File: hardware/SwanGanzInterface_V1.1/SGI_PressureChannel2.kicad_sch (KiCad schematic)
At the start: 18 parts, among them J6 Conn_01x04_Pin, U12 INA122D, U13 OPA2350

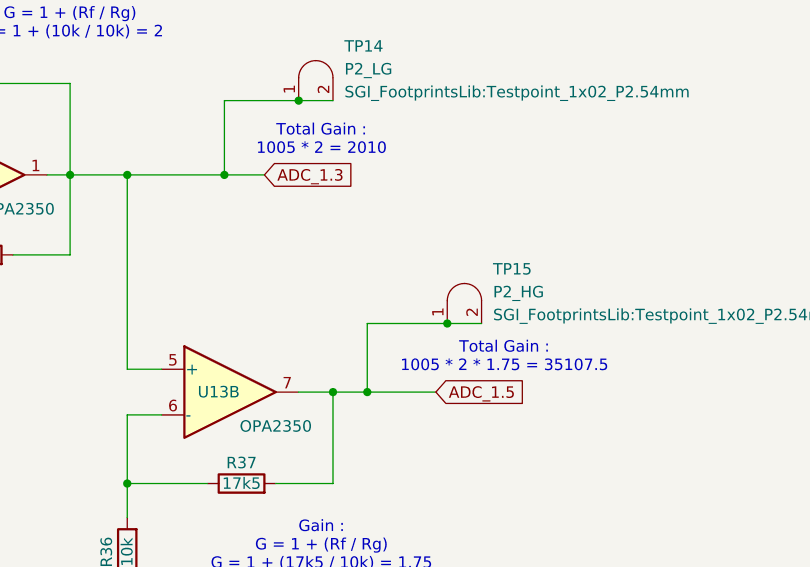
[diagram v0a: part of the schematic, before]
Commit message: Pin Allocation, updated schematic with new pins, reassigned
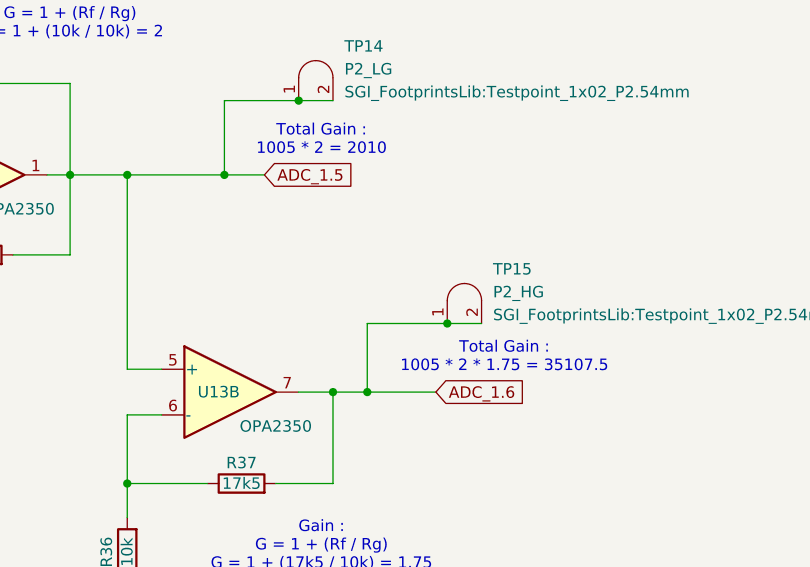
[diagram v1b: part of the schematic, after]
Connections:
- net ADC_1.3 is gone; now on net ADC_1.5: C20.2, R35.2, TP14.1 (A), TP14.2 (B), U13.1, U13.5 (+)
- net ADC_1.5: no longer R37.2, TP15.1 (A), TP15.2 (B), U13.7
- new net ADC_1.6: R37.2, TP15.1 (A), TP15.2 (B), U13.7
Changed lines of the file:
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@@
 		)
 	)
-	(global_label "ADC_1.5"
+	(global_label "ADC_1.6"
 		(shape input)
 		(at 201.93 88.9 0)
@@
 		)
 	)
-	(global_label "ADC_1.3"
+	(global_label "ADC_1.5"
 		(shape input)
 		(at 182.88 64.77 0)

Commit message: Hooked up MSP
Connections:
- net ADC_1.5 renamed P2_LG_ADC_1.5
- net ADC_1.6 renamed P2_HG_ADC_1.6
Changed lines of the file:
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@@
 		)
 	)
-	(global_label "ADC_1.6"
+	(global_label "P2_HG_ADC_1.6"
 		(shape input)
 		(at 201.93 88.9 0)
@@
 		)
 		(property "Intersheetrefs" "${INTERSHEET_REFS}"
-			(at 212.5352 88.9 0)
+			(at 219.5504 88.9 0)
 			(effects
 				(font
@@
 		)
 	)
-	(global_label "ADC_1.5"
+	(global_label "P2_LG_ADC_1.5"
 		(shape input)
 		(at 182.88 64.77 0)
@@
 		)
 		(property "Intersheetrefs" "${INTERSHEET_REFS}"
-			(at 193.4852 64.77 0)
+			(at 200.198 64.77 0)
 			(effects
 				(font

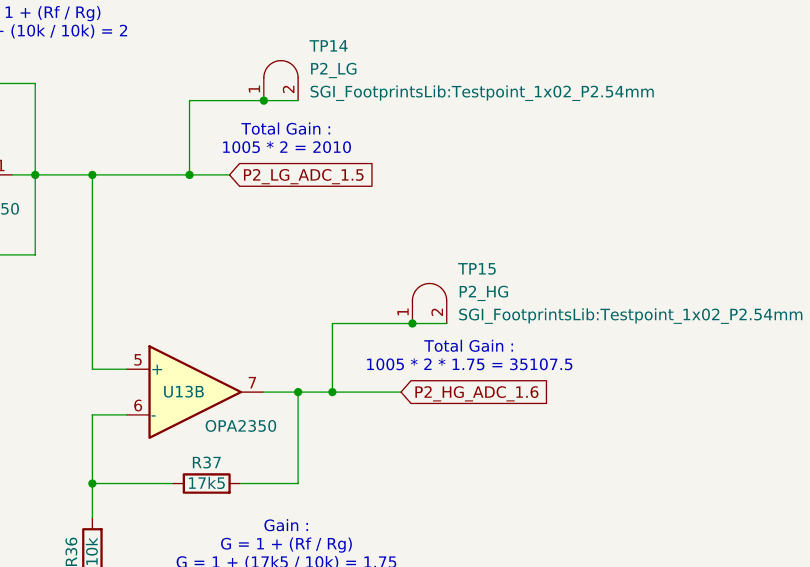
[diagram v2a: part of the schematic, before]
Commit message: Started converting things to use touch screen chip
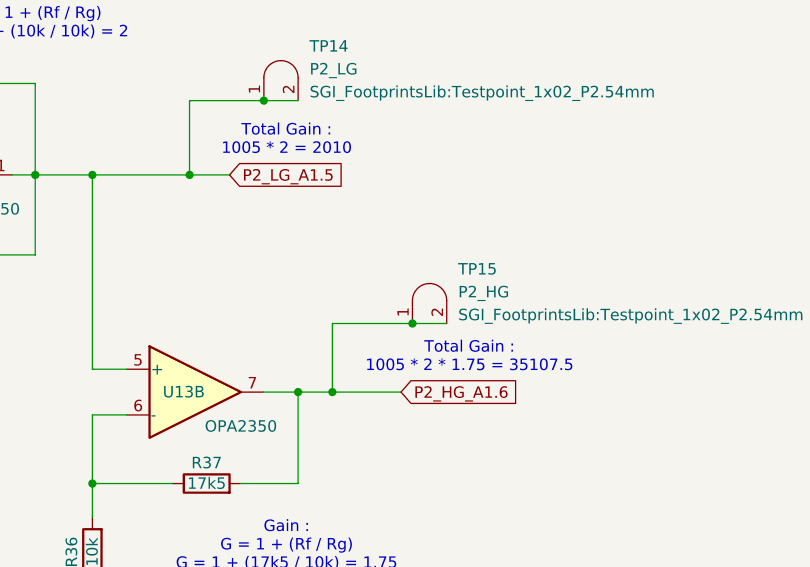
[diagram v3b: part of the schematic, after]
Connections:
- net P2_HG_ADC_1.6 renamed P2_HG_A1.6
- net P2_LG_ADC_1.5 renamed P2_LG_A1.5
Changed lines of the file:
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@@
 		)
 	)
-	(global_label "P2_HG_ADC_1.6"
+	(global_label "P2_HG_A1.6"
 		(shape input)
 		(at 201.93 88.9 0)
@@
 		)
 		(property "Intersheetrefs" "${INTERSHEET_REFS}"
-			(at 219.5504 88.9 0)
+			(at 216.0428 88.9 0)
 			(effects
 				(font
@@
 		)
 	)
-	(global_label "P2_LG_ADC_1.5"
+	(global_label "P2_LG_A1.5"
 		(shape input)
 		(at 182.88 64.77 0)
@@
 		)
 		(property "Intersheetrefs" "${INTERSHEET_REFS}"
-			(at 200.198 64.77 0)
+			(at 196.6904 64.77 0)
 			(effects
 				(font

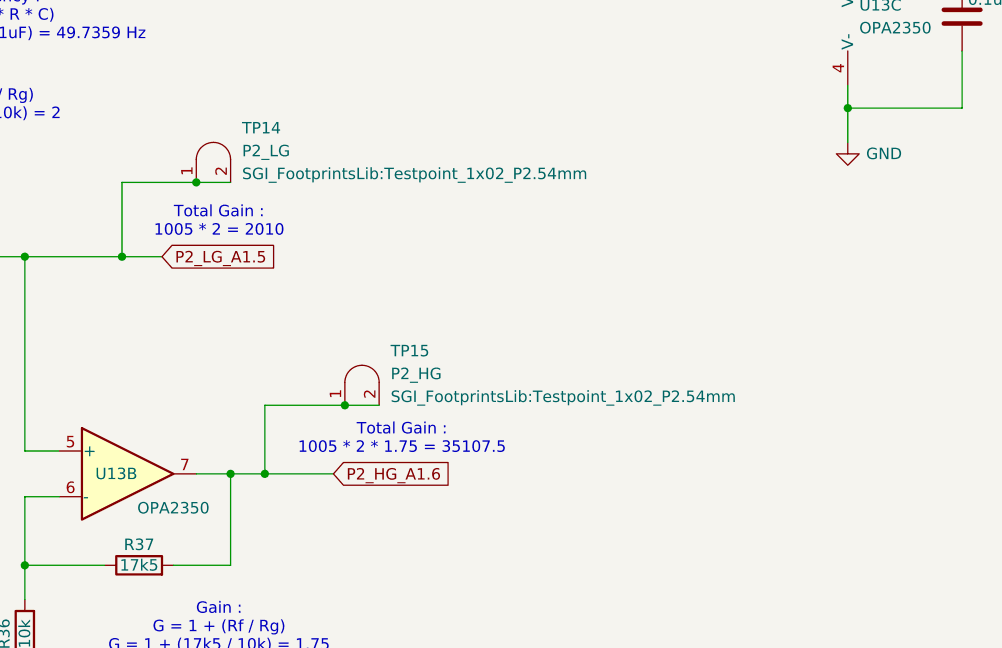
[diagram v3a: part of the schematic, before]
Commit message: Got 64 pin MSP symbol and footprint and started implementation
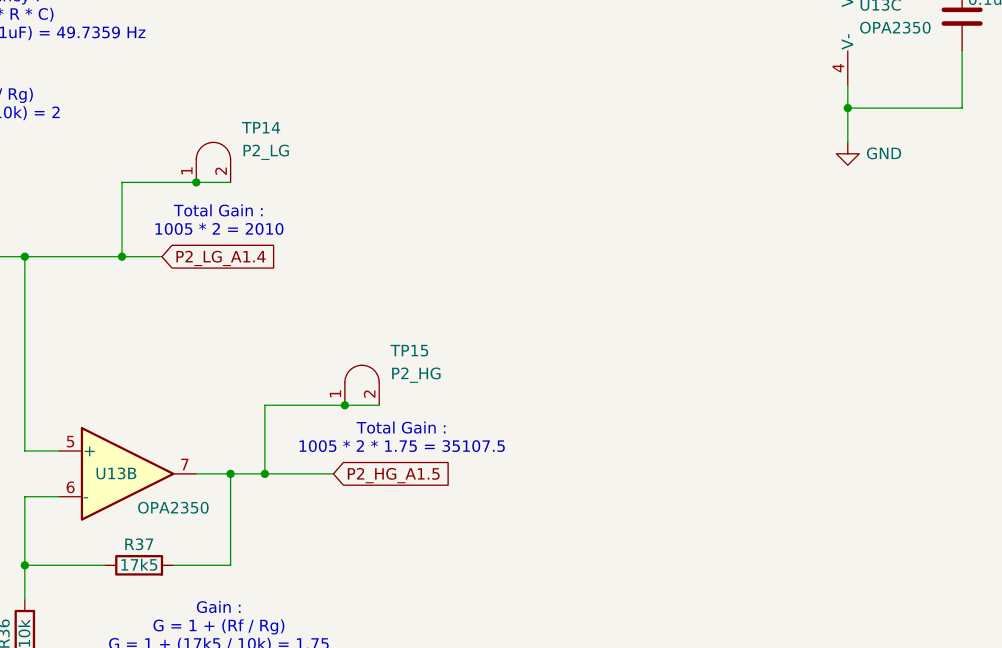
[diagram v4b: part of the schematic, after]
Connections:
- net P2_HG_A1.6 renamed P2_HG_A1.5
- net P2_LG_A1.5 renamed P2_LG_A1.4
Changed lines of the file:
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@@
 		)
 	)
-	(global_label "P2_HG_A1.6"
+	(global_label "P2_HG_A1.5"
 		(shape input)
 		(at 201.93 88.9 0)
@@
 		)
 	)
-	(global_label "P2_LG_A1.5"
+	(global_label "P2_LG_A1.4"
 		(shape input)
 		(at 182.88 64.77 0)
@@
 				)
 				(justify left)
+				(hide yes)
 			)
 		)
@@
 				)
 				(justify left)
-			)
-		)
+				(hide yes)
+			)
+		)

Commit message: Schematic Check
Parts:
- renumbered C18 to C23, C19 to C24, C20 to C25, C21 to C26, R31 to R29, R32 to R30, R33 to R31, R34 to R32, R35 to R33, R36 to R34, R37 to R35, U13 to U10, U12 to U9
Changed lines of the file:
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@@
 		(on_board yes)
 		(dnp no)
-		(property "Reference" "#PWR068"
+		(property "Reference" "#PWR066"
 			(at 259.08 27.94 0)
 			(effects
@@
 			(project "SwanGanzInterface"
 				(path "/4e9a6e30-f660-472b-9696-bea1f34b4545/5b443651-3bea-4d19-bd25-a234ca65ad96"
-					(reference "#PWR068")
+					(reference "#PWR066")
 					(unit 1)
 				)
@@
 		(dnp no)
 		(fields_autoplaced yes)
-		(property "Reference" "U13"
+		(property "Reference" "U10"
 			(at 260.35 36.8299 0)
 			(effects
@@
 			(project "SwanGanzInterface"
 				(path "/4e9a6e30-f660-472b-9696-bea1f34b4545/5b443651-3bea-4d19-bd25-a234ca65ad96"
-					(reference "U13")
+					(reference "U10")
 					(unit 3)
 				)
@@
 		(on_board yes)
 		(dnp no)
-		(property "Reference" "#PWR059"
+		(property "Reference" "#PWR057"
 			(at 29.21 200.66 0)
 			(effects
@@
 			(project "SwanGanzInterface"
 				(path "/4e9a6e30-f660-472b-9696-bea1f34b4545/5b443651-3bea-4d19-bd25-a234ca65ad96"
-					(reference "#PWR059")
+					(reference "#PWR057")
 					(unit 1)
 				)
@@
 		(on_board yes)
 		(dnp no)
-		(property "Reference" "#PWR067"
+		(property "Reference" "#PWR065"
 			(at 167.64 118.11 0)
 			(effects
@@
 			(project "SwanGanzInterface"
 				(path "/4e9a6e30-f660-472b-9696-bea1f34b4545/5b443651-3bea-4d19-bd25-a234ca65ad96"
-					(reference "#PWR067")
+					(reference "#PWR065")
 					(unit 1)
 				)
@@
 		(on_board yes)
 		(dnp no)
-		(property "Reference" "R35"
+		(property "Reference" "R33"
 			(at 151.13 71.755 90)
 			(effects
@@
 			(project "SwanGanzInterface"
 				(path "/4e9a6e30-f660-472b-9696-bea1f34b4545/5b443651-3bea-4d19-bd25-a234ca65ad96"
-					(reference "R35")
+					(reference "R33")
 					(unit 1)
 				)
@@
 		(on_board yes)
 		(dnp no)
-		(property "Reference" "R32"
+		(property "Reference" "R30"
 			(at 115.57 60.325 90)
 			(effects
@@
 			(project "SwanGanzInterface"
 				(path "/4e9a6e30-f660-472b-9696-bea1f34b4545/5b443651-3bea-4d19-bd25-a234ca65ad96"
-					(reference "R32")
+					(reference "R30")
 					(unit 1)
 				)
@@
 		(on_board yes)
 		(dnp no)
-		(property "Reference" "#PWR065"
+		(property "Reference" "#PWR063"
 			(at 132.715 81.28 0)
 			(effects
@@
 			(project "SwanGanzInterface"
 				(path "/4e9a6e30-f660-472b-9696-bea1f34b4545/5b443651-3bea-4d19-bd25-a234ca65ad96"
-					(reference "#PWR065")
+					(reference "#PWR063")
 					(unit 1)
 				)
@@
 		(on_board yes)
 		(dnp no)
-		(property "Reference" "#PWR066"
+		(property "Reference" "#PWR064"
 			(at 139.7 93.98 0)
 			(effects
@@
 			(project "SwanGanzInterface"
 				(path "/4e9a6e30-f660-472b-9696-bea1f34b4545/5b443651-3bea-4d19-bd25-a234ca65ad96"
-					(reference "#PWR066")
+					(reference "#PWR064")
 					(unit 1)
 				)
@@
 		(on_board yes)
 		(dnp no)
-		(property "Reference" "R34"
+		(property "Reference" "R32"
 			(at 137.795 80.01 90)
 			(effects
@@
 			(project "SwanGanzInterface"
 				(path "/4e9a6e30-f660-472b-9696-bea1f34b4545/5b443651-3bea-4d19-bd25-a234ca65ad96"
-					(reference "R34")
+					(reference "R32")
 					(unit 1)
 				)
@@
 		(on_board yes)
 		(dnp no)
-		(property "Reference" "R31"
+		(property "Reference" "R29"
 			(at 95.25 44.704 90)
 			(effects
@@
 			(project "SwanGanzInterface"
 				(path "/4e9a6e30-f660-472b-9696-bea1f34b4545/5b443651-3bea-4d19-bd25-a234ca65ad96"
-					(reference "R31")
+					(reference "R29")
 					(unit 1)
 				)
@@
 				)
 				(justify left)
+				(hide yes)
 			)
 		)
@@
 		(on_board yes)
 		(dnp no)
-		(property "Reference" "C21"
+		(property "Reference" "C26"
 			(at 272.415 34.29 0)
 			(effects
@@
 			(project "SwanGanzInterface"
 				(path "/4e9a6e30-f660-472b-9696-bea1f34b4545/5b443651-3bea-4d19-bd25-a234ca65ad96"
-					(reference "C21")
+					(reference "C26")
 					(unit 1)
 				)
@@
 		(on_board yes)
 		(dnp no)
-		(property "Reference" "U13"
+		(property "Reference" "U10"
 			(at 148.59 64.77 0)
 			(effects
@@
 			(project "SwanGanzInterface"
 				(path "/4e9a6e30-f660-472b-9696-bea1f34b4545/5b443651-3bea-4d19-bd25-a234ca65ad96"
-					(reference "U13")
+					(reference "U10")
 					(unit 1)
 				)
@@
 		(on_board yes)
 		(dnp no)
-		(property "Reference" "#PWR062"
+		(property "Reference" "#PWR060"
 			(at 83.82 88.9 0)
 			(effects
@@
 			(project "SwanGanzInterface"
 				(path "/4e9a6e30-f660-472b-9696-bea1f34b4545/5b443651-3bea-4d19-bd25-a234ca65ad96"
-					(reference "#PWR062")
+					(reference "#PWR060")
 					(unit 1)
 				)
@@
 		(on_board yes)
 		(dnp no)
-		(property "Reference" "U12"
+		(property "Reference" "U9"
 			(at 91.186 62.23 0)
 			(effects
@@
 			(project "SwanGanzInterface"
 				(path "/4e9a6e30-f660-472b-9696-bea1f34b4545/5b443651-3bea-4d19-bd25-a234ca65ad96"
-					(reference "U12")
+					(reference "U9")
 					(unit 1)
 				)
@@
 		(on_board yes)
 		(dnp no)
-		(property "Reference" "R33"
+		(property "Reference" "R31"
 			(at 127 60.325 90)
 			(effects
@@
 			(project "SwanGanzInterface"
 				(path "/4e9a6e30-f660-472b-9696-bea1f34b4545/5b443651-3bea-4d19-bd25-a234ca65ad96"
-					(reference "R33")
+					(reference "R31")
 					(unit 1)
 				)
@@
 		(on_board yes)
 		(dnp no)
-		(property "Reference" "R37"
+		(property "Reference" "R35"
 			(at 180.34 96.774 90)
 			(effects
@@
 			(project "SwanGanzInterface"
 				(path "/4e9a6e30-f660-472b-9696-bea1f34b4545/5b443651-3bea-4d19-bd25-a234ca65ad96"
-					(reference "R37")
+					(reference "R35")
 					(unit 1)
 				)
@@
 		(dnp no)
 		(fields_autoplaced yes)
-		(property "Reference" "#PWR069"
+		(property "Reference" "#PWR067"
 			(at 259.08 58.42 0)
 			(effects
@@
 			(project "SwanGanzInterface"
 				(path "/4e9a6e30-f660-472b-9696-bea1f34b4545/5b443651-3bea-4d19-bd25-a234ca65ad96"
-					(reference "#PWR069")
+					(reference "#PWR067")
 					(unit 1)
 				)
@@
 		(on_board yes)
 		(dnp no)
-		(property "Reference" "#PWR061"
+		(property "Reference" "#PWR059"
 			(at 83.82 39.37 0)
 			(effects
@@
 			(project "SwanGanzInterface"
 				(path "/4e9a6e30-f660-472b-9696-bea1f34b4545/5b443651-3bea-4d19-bd25-a234ca65ad96"
-					(reference "#PWR061")
+					(reference "#PWR059")
 					(unit 1)
 				)
@@
 		(dnp no)
 		(fields_autoplaced yes)
-		(property "Reference" "#PWR063"
+		(property "Reference" "#PWR061"
 			(at 96.52 46.99 0)
 			(effects
@@
 			(project "SwanGanzInterface"
 				(path "/4e9a6e30-f660-472b-9696-bea1f34b4545/5b443651-3bea-4d19-bd25-a234ca65ad96"
-					(reference "#PWR063")
+					(reference "#PWR061")
 					(unit 1)
 				)
@@
 		(on_board yes)
 		(dnp no)
-		(property "Reference" "#PWR060"
+		(property "Reference" "#PWR058"
 			(at 49.53 78.74 0)
 			(effects
@@
 			(project "SwanGanzInterface"
 				(path "/4e9a6e30-f660-472b-9696-bea1f34b4545/5b443651-3bea-4d19-bd25-a234ca65ad96"
-					(reference "#PWR060")
+					(reference "#PWR058")
 					(unit 1)
 				)
@@
 		(on_board yes)
 		(dnp no)
-		(property "Reference" "#PWR064"
+		(property "Reference" "#PWR062"
 			(at 96.52 83.82 0)
 			(effects
@@
 			(project "SwanGanzInterface"
 				(path "/4e9a6e30-f660-472b-9696-bea1f34b4545/5b443651-3bea-4d19-bd25-a234ca65ad96"
-					(reference "#PWR064")
+					(reference "#PWR062")
 					(unit 1)
 				)
@@
 		(on_board yes)
 		(dnp no)
-		(property "Reference" "U13"
+		(property "Reference" "U10"
 			(at 177.8 88.9 0)
 			(effects
@@
 			(project "SwanGanzInterface"
 				(path "/4e9a6e30-f660-472b-9696-bea1f34b4545/5b443651-3bea-4d19-bd25-a234ca65ad96"
-					(reference "U13")
+					(reference "U10")
 					(unit 2)
 				)
@@
 		(on_board yes)
 		(dnp no)
-		(property "Reference" "C20"
+		(property "Reference" "C25"
 			(at 145.796 52.578 90)
 			(effects
@@
 			(project "SwanGanzInterface"
 				(path "/4e9a6e30-f660-472b-9696-bea1f34b4545/5b443651-3bea-4d19-bd25-a234ca65ad96"
-					(reference "C20")
+					(reference "C25")
 					(unit 1)
 				)
@@
 		(on_board yes)
 		(dnp no)
-		(property "Reference" "C19"
+		(property "Reference" "C24"
 			(at 133.35 67.31 0)
 			(effects
@@
 			(project "SwanGanzInterface"
 				(path "/4e9a6e30-f660-472b-9696-bea1f34b4545/5b443651-3bea-4d19-bd25-a234ca65ad96"
-					(reference "C19")
+					(reference "C24")
 					(unit 1)
 				)
@@
 		(on_board yes)
 		(dnp no)
-		(property "Reference" "C18"
+		(property "Reference" "C23"
 			(at 90.17 34.29 90)
 			(effects
@@
 			(project "SwanGanzInterface"
 				(path "/4e9a6e30-f660-472b-9696-bea1f34b4545/5b443651-3bea-4d19-bd25-a234ca65ad96"
-					(reference "C18")
+					(reference "C23")
 					(unit 1)
 				)
@@
 		(on_board yes)
 		(dnp no)
-		(property "Reference" "R36"
+		(property "Reference" "R34"
 			(at 165.354 106.68 90)
 			(effects
@@
 			(project "SwanGanzInterface"
 				(path "/4e9a6e30-f660-472b-9696-bea1f34b4545/5b443651-3bea-4d19-bd25-a234ca65ad96"
-					(reference "R36")
-					(unit 1)
-				)
+					(reference "R34")
+					(unit 1)
+				)
